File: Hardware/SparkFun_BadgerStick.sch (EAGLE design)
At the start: 38 parts, among them Q1 DMG2307L, U1 MIC5205-3.3V, U2 ATMEGA328P_TQFP, U3 CY7C65213, Y1 4MHz

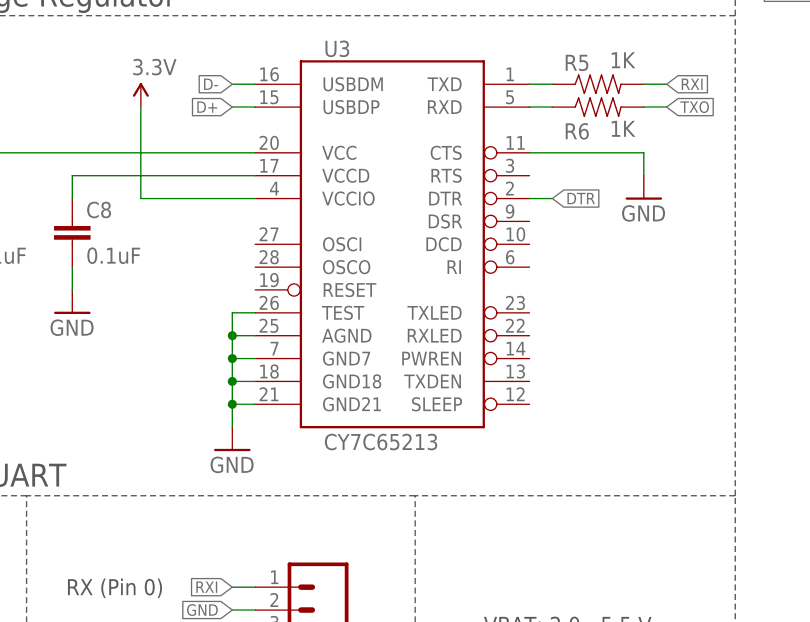
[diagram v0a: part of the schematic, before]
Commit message: Switched Cypress USB-Serial bridge to FT232RL
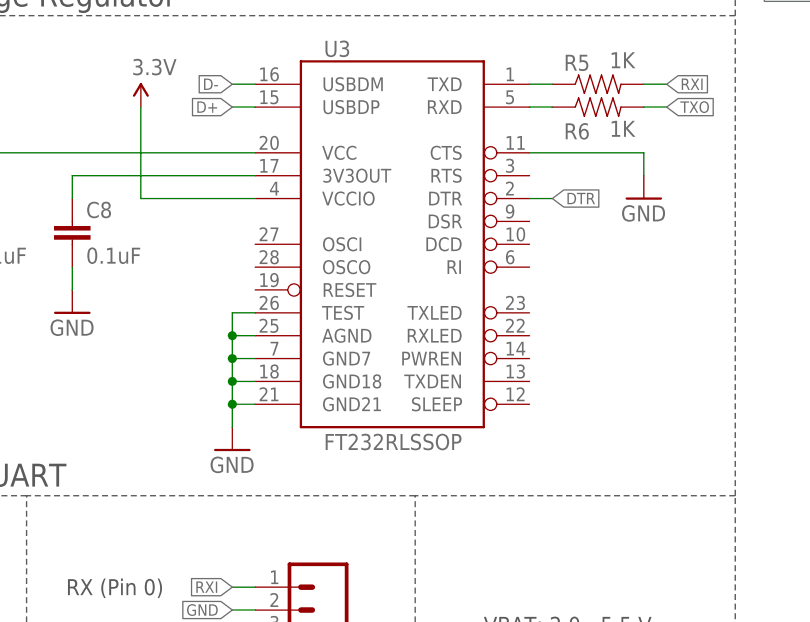
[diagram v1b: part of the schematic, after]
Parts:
- U3: value CY7C65213 -> FT232RLSSOP; device SparkFun-DigitalIC:CY7C65213 -> SparkFun-DigitalIC:FT232RLSSOP
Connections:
- net N$2: now also U3.3V3OUT; no longer U3.VCCD
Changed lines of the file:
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@@
 <setting verticaltext="up"/>
 </settings>
-<grid distance="0.1" unitdist="inch" unit="inch" style="lines" multiple="1" display="yes" altdistance="0.01" altunitdist="inch" altunit="inch"/>
+<grid distance="0.1" unitdist="inch" unit="inch" style="lines" multiple="1" display="no" altdistance="0.01" altunitdist="inch" altunit="inch"/>
 <layers>
 <layer number="1" name="Top" color="4" fill="1" visible="no" active="no"/>
@@
 <part name="D3" library="SparkFun-LED" deviceset="LED-GREEN" device="0603" value="GREEN"/>
 <part name="GND12" library="SparkFun-Aesthetics" deviceset="GND" device=""/>
-<part name="U3" library="SparkFun-DigitalIC" deviceset="CY7C65213" device=""/>
+<part name="U3" library="SparkFun-DigitalIC" deviceset="FT232RL" device="SSOP"/>
 <part name="C7" library="SparkFun-Capacitors" deviceset="0.1UF-25V(+80/-20%)(0603)" device="" value="0.1uF"/>
 <part name="C8" library="SparkFun-Capacitors" deviceset="0.1UF-25V(+80/-20%)(0603)" device="" value="0.1uF"/>
@@
 <net name="N$2" class="0">
 <segment>
-<pinref part="U3" gate="G$1" pin="VCCD"/>
+<pinref part="U3" gate="G$1" pin="3V3OUT"/>
 <wire x1="88.9" y1="116.84" x2="68.58" y2="116.84" width="0.1524" layer="91"/>
 <pinref part="C8" gate="G$1" pin="1"/>
